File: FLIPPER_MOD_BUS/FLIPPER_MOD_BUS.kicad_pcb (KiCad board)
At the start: 2 copper layers, 62.8 x 23.2 mm, 27 parts, among them J1 Conn_01x02, J2 Conn_01x10_Socket, J3 Conn_01x08_Socket, J4 Conn_01x02_Socket, U1 SP3485EN

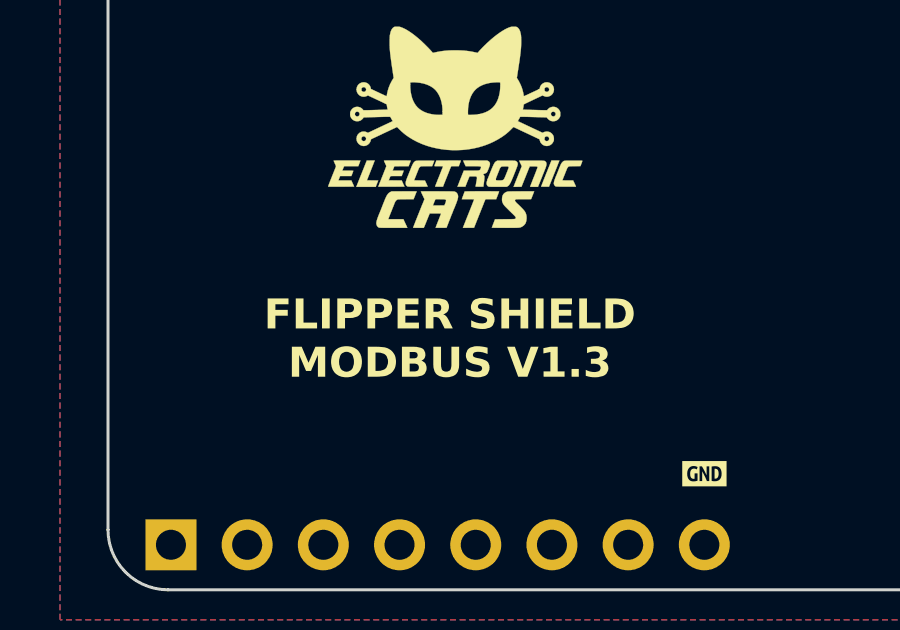
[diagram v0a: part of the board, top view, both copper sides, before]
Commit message: feat: rename addons
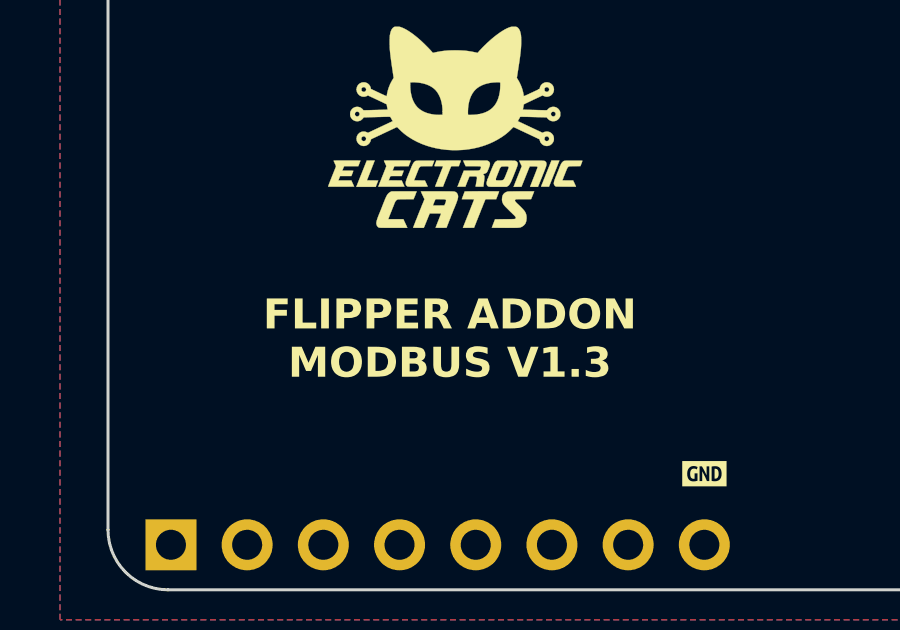
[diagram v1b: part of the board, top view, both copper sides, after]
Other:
- board text added: "FLIPPER ADDON MODBUS V1.3"
- board text removed: "FLIPPER SHIELD MODBUS V1.3"
